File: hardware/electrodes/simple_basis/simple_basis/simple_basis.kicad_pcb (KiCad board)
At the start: 2 copper layers, 58.4 x 69.7 mm, 0 parts

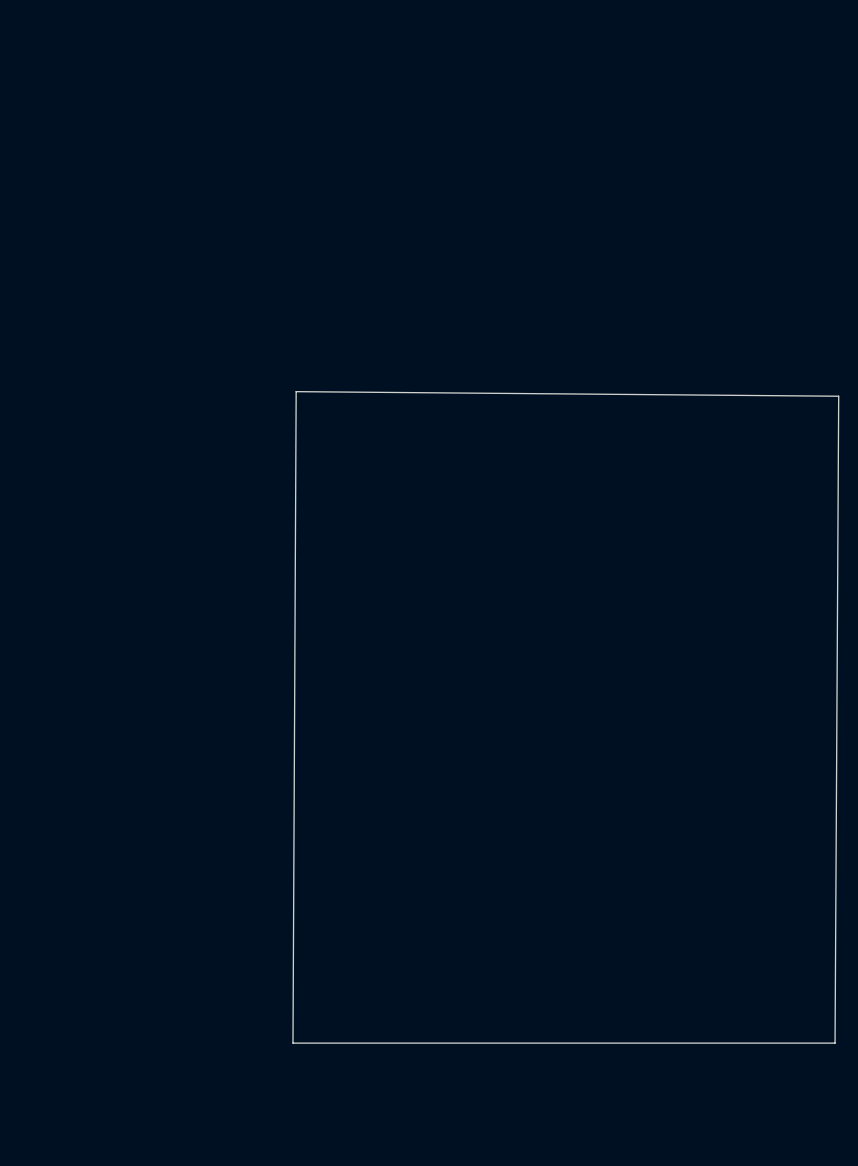
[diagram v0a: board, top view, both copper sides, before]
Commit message: Generating simple electrodes
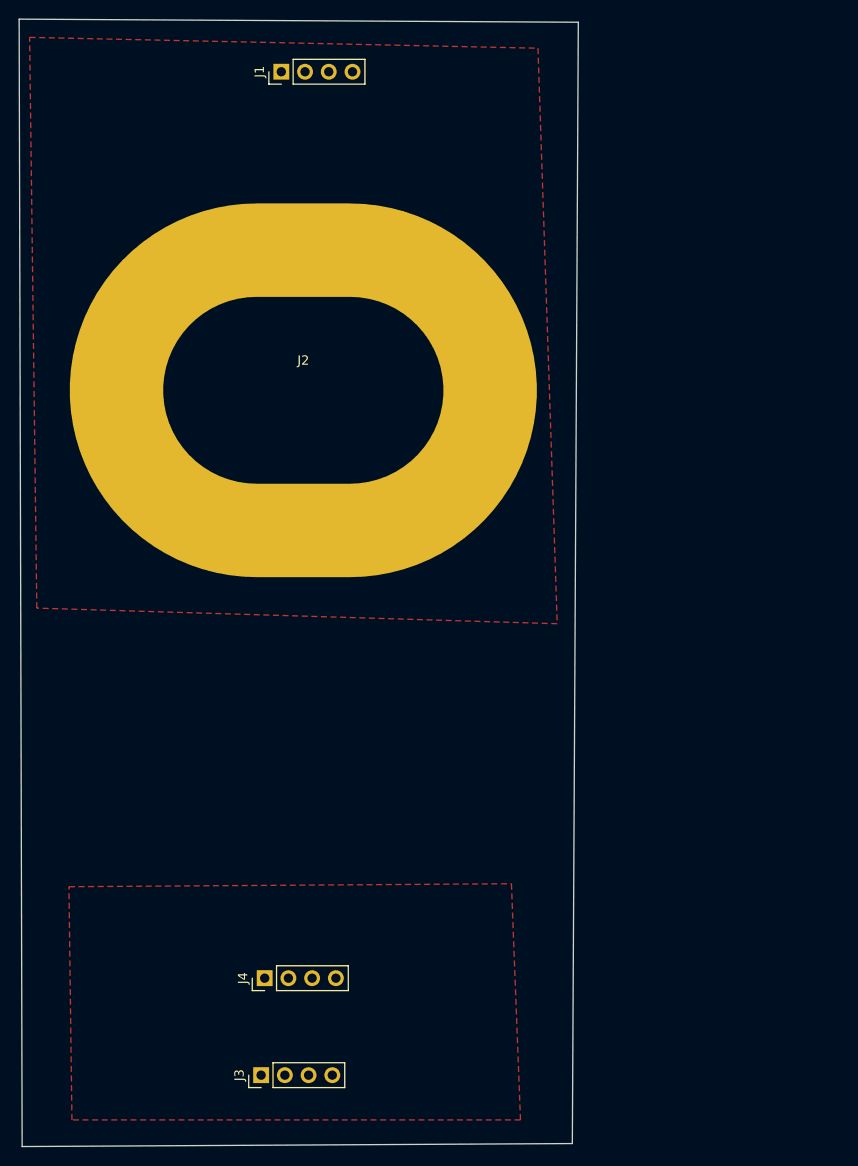
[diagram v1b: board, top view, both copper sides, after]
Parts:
- added J1: Conn_01x04_Male, Connector_PinHeader_2.54mm:PinHeader_1x04_P2.54mm_Vertical, F.Cu at (128.1, 45.5)
- added J2: Metallic_Electrode, electrodes:Electrode_ThroughHole_V0.1, F.Cu at (130.4, 75.9)
- added J3: Conn_01x04_Male, Connector_PinHeader_2.54mm:PinHeader_1x04_P2.54mm_Vertical, F.Cu at (125.9, 152.9)
- added J4: Conn_01x04_Male, Connector_PinHeader_2.54mm:PinHeader_1x04_P2.54mm_Vertical, F.Cu at (126.3, 142.6)
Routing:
- added copper zone on F.Cu, net Net-(J1-Pad1)
- added copper zone on F.Cu, net Net-(J3-Pad1)
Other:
- board size 58.4 x 69.7 mm -> 59.8 x 120.7 mm
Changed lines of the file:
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@@
     (tracks 0)
     (zones 0)
-    (modules 0)
-    (nets 1)
+    (modules 4)
+    (nets 3)
   )
   (page A4)
@@
     (visible_elements FFFFFF7F)
     (pcbplotparams
-      (layerselection 0x010fc_ffffffff)
+      (layerselection 0x010f0_ffffffff)
       (usegerberextensions false)
       (usegerberattributes true)
@@
       (outputformat 1)
       (mirror false)
-      (drillshape 1)
+      (drillshape 0)
       (scaleselection 1)
-      (outputdirectory ""))
+      (outputdirectory "../gerber/"))
   )
   (net 0 "")
+  (net 1 "Net-(J1-Pad1)")
+  (net 2 "Net-(J3-Pad1)")
   (net_class Default "This is the default net class."
     (clearance 0.2)
@@
     (uvia_dia 0.3)
     (uvia_drill 0.1)
-  )
-  (gr_line (start 129.65 79.79) (end 187.72 80.28) (layer Edge.Cuts) (width 0.1))
-  (gr_line (start 129.31 149.52) (end 129.65 79.79) (layer Edge.Cuts) (width 0.1))
-  (gr_line (start 187.33 149.52) (end 129.31 149.52) (layer Edge.Cuts) (width 0.1))
-  (gr_line (start 187.72 80.28) (end 187.33 149.52) (layer Edge.Cuts) (width 0.1))
+    (add_net "Net-(J1-Pad1)")
+    (add_net "Net-(J3-Pad1)")
+  )
+  (module Connector_PinHeader_2.54mm:PinHeader_1x04_P2.54mm_Vertical (layer F.Cu)
+    (at 126.28 142.57 90)
+    (descr "Through hole straight pin header, 1x04, 2.54mm pitch, single row")
+    (tags "Through hole pin header THT 1x04 2.54mm single row")
+    (fp_text reference J4 (at 0 -2.33 90) (layer F.SilkS)
+      (effects (font (size 1 1) (thickness 0.15)))
+    )
+    (fp_text value Conn_01x04_Male (at 0 9.95 90) (layer F.Fab)
+      (effects (font (size 1 1) (thickness 0.15)))
+    )
+    (fp_text user %R (at 0 3.81) (layer F.Fab)
+      (effects (font (size 1 1) (thickness 0.15)))
+    )
+    (fp_line (start -0.635 -1.27) (end 1.27 -1.27) (layer F.Fab) (width 0.1))
+    (fp_line (start 1.27 -1.27) (end 1.27 8.89) (layer F.Fab) (width 0.1))
+    (fp_line (start 1.27 8.89) (end -1.27 8.89) (layer F.Fab) (width 0.1))
+    (fp_line (start -1.27 8.89) (end -1.27 -0.635) (layer F.Fab) (width 0.1))
+    (fp_line (start -1.27 -0.635) (end -0.635 -1.27) (layer F.Fab) (width 0.1))
+    (fp_line (start -1.33 8.95) (end 1.33 8.95) (layer F.SilkS) (width 0.12))
+    (fp_line (start -1.33 1.27) (end -1.33 8.95) (layer F.SilkS) (width 0.12))
+    (fp_line (start 1.33 1.27) (end 1.33 8.95) (layer F.SilkS) (width 0.12))
+    (fp_line (start -1.33 1.27) (end 1.33 1.27) (layer F.SilkS) (width 0.12))
+    (fp_line (start -1.33 0) (end -1.33 -1.33) (layer F.SilkS) (width 0.12))
+    (fp_line (start -1.33 -1.33) (end 0 -1.33) (layer F.SilkS) (width 0.12))
+    (fp_line (start -1.8 -1.8) (end -1.8 9.4) (layer F.CrtYd) (width 0.05))
+    (fp_line (start -1.8 9.4) (end 1.8 9.4) (layer F.CrtYd) (width 0.05))
+    (fp_line (start 1.8 9.4) (end 1.8 -1.8) (layer F.CrtYd) (width 0.05))
+    (fp_line (start 1.8 -1.8) (end -1.8 -1.8) (layer F.CrtYd) (width 0.05))
+    (pad 4 thru_hole oval (at 0 7.62 90) (size 1.7 1.7) (drill 1) (layers *.Cu *.Mask)
+      (net 2 "Net-(J3-Pad1)"))
+    (pad 3 thru_hole oval (at 0 5.08 90) (size 1.7 1.7) (drill 1) (layers *.Cu *.Mask)
+      (net 2 "Net-(J3-Pad1)"))
+    (pad 2 thru_hole oval (at 0 2.54 90) (size 1.7 1.7) (drill 1) (layers *.Cu *.Mask)
+      (net 2 "Net-(J3-Pad1)"))
+    (pad 1 thru_hole rect (at 0 0 90) (size 1.7 1.7) (drill 1) (layers *.Cu *.Mask)
+      (net 2 "Net-(J3-Pad1)"))
+    (model ${KISYS3DMOD}/Connector_PinHeader_2.54mm.3dshapes/PinHeader_1x04_P2.54mm_Vertical.wrl
+      (at (xyz 0 0 0))
+      (scale (xyz 1 1 1))
+      (rotate (xyz 0 0 0))
+    )
+  )
+  (module Connector_PinHeader_2.54mm:PinHeader_1x04_P2.54mm_Vertical (layer F.Cu)
+    (at 125.9 152.95 90)
+    (descr "Through hole straight pin header, 1x04, 2.54mm pitch, single row")
+    (tags "Through hole pin header THT 1x04 2.54mm single row")
+    (fp_text reference J3 (at 0 -2.33 90) (layer F.SilkS)
+      (effects (font (size 1 1) (thickness 0.15)))
+    )
+    (fp_text value Conn_01x04_Male (at 0 9.95 90) (layer F.Fab)
+      (effects (font (size 1 1) (thickness 0.15)))
+    )
+    (fp_text user %R (at 0 3.81) (layer F.Fab)
+      (effects (font (size 1 1) (thickness 0.15)))
+    )
+    (fp_line (start -0.635 -1.27) (end 1.27 -1.27) (layer F.Fab) (width 0.1))
+    (fp_line (start 1.27 -1.27) (end 1.27 8.89) (layer F.Fab) (width 0.1))
+    (fp_line (start 1.27 8.89) (end -1.27 8.89) (layer F.Fab) (width 0.1))
+    (fp_line (start -1.27 8.89) (end -1.27 -0.635) (layer F.Fab) (width 0.1))
+    (fp_line (start -1.27 -0.635) (end -0.635 -1.27) (layer F.Fab) (width 0.1))
+    (fp_line (start -1.33 8.95) (end 1.33 8.95) (layer F.SilkS) (width 0.12))
+    (fp_line (start -1.33 1.27) (end -1.33 8.95) (layer F.SilkS) (width 0.12))
+    (fp_line (start 1.33 1.27) (end 1.33 8.95) (layer F.SilkS) (width 0.12))
+    (fp_line (start -1.33 1.27) (end 1.33 1.27) (layer F.SilkS) (width 0.12))
+    (fp_line (start -1.33 0) (end -1.33 -1.33) (layer F.SilkS) (width 0.12))
+    (fp_line (start -1.33 -1.33) (end 0 -1.33) (layer F.SilkS) (width 0.12))
+    (fp_line (start -1.8 -1.8) (end -1.8 9.4) (layer F.CrtYd) (width 0.05))
+    (fp_line (start -1.8 9.4) (end 1.8 9.4) (layer F.CrtYd) (width 0.05))
+    (fp_line (start 1.8 9.4) (end 1.8 -1.8) (layer F.CrtYd) (width 0.05))
+    (fp_line (start 1.8 -1.8) (end -1.8 -1.8) (layer F.CrtYd) (width 0.05))
+    (pad 4 thru_hole oval (at 0 7.62 90) (size 1.7 1.7) (drill 1) (layers *.Cu *.Mask)
+      (net 2 "Net-(J3-Pad1)"))
+    (pad 3 thru_hole oval (at 0 5.08 90) (size 1.7 1.7) (drill 1) (layers *.Cu *.Mask)
+      (net 2 "Net-(J3-Pad1)"))
+    (pad 2 thru_hole oval (at 0 2.54 90) (size 1.7 1.7) (drill 1) (layers *.Cu *.Mask)
+      (net 2 "Net-(J3-Pad1)"))
+    (pad 1 thru_hole rect (at 0 0 90) (size 1.7 1.7) (drill 1) (layers *.Cu *.Mask)
+      (net 2 "Net-(J3-Pad1)"))
+    (model ${KISYS3DMOD}/Connector_PinHeader_2.54mm.3dshapes/PinHeader_1x04_P2.54mm_Vertical.wrl
+      (at (xyz 0 0 0))
+      (scale (xyz 1 1 1))
+      (rotate (xyz 0 0 0))
+    )
+  )
+  (module electrodes:Electrode_ThroughHole_V0.1 (layer F.Cu)
+    (at 130.414999 75.944999)
+    (fp_text reference J2 (at 0 0.5) (layer F.SilkS)
+      (effects (font (size 1 1) (thickness 0.15)))
+    )
+    (fp_text value Metallic_Electrode (at 0 -0.5) (layer F.Fab)
+      (effects (font (size 1 1) (thickness 0.15)))
+    )
+    (pad 1 thru_hole oval (at 0 3.7) (size 50 40) (drill oval 30 20) (layers *.Cu *.Mask)
+      (net 1 "Net-(J1-Pad1)"))
+  )
+  (module Connector_PinHeader_2.54mm:PinHeader_1x04_P2.54mm_Vertical (layer F.Cu)
+    (at 128.06 45.55 90)
+    (descr "Through hole straight pin header, 1x04, 2.54mm pitch, single row")
+    (tags "Through hole pin header THT 1x04 2.54mm single row")
+    (fp_text reference J1 (at 0 -2.33 90) (layer F.SilkS)
+      (effects (font (size 1 1) (thickness 0.15)))
+    )
+    (fp_text value Conn_01x04_Male (at 0 9.95 90) (layer F.Fab)
+      (effects (font (size 1 1) (thickness 0.15)))
+    )
+    (fp_text user %R (at 0 3.81) (layer F.Fab)
+      (effects (font (size 1 1) (thickness 0.15)))
+    )
+    (fp_line (start -0.635 -1.27) (end 1.27 -1.27) (layer F.Fab) (width 0.1))
+    (fp_line (start 1.27 -1.27) (end 1.27 8.89) (layer F.Fab) (width 0.1))
+    (fp_line (start 1.27 8.89) (end -1.27 8.89) (layer F.Fab) (width 0.1))
+    (fp_line (start -1.27 8.89) (end -1.27 -0.635) (layer F.Fab) (width 0.1))
+    (fp_line (start -1.27 -0.635) (end -0.635 -1.27) (layer F.Fab) (width 0.1))
+    (fp_line (start -1.33 8.95) (end 1.33 8.95) (layer F.SilkS) (width 0.12))
+    (fp_line (start -1.33 1.27) (end -1.33 8.95) (layer F.SilkS) (width 0.12))
+    (fp_line (start 1.33 1.27) (end 1.33 8.95) (layer F.SilkS) (width 0.12))
+    (fp_line (start -1.33 1.27) (end 1.33 1.27) (layer F.SilkS) (width 0.12))
+    (fp_line (start -1.33 0) (end -1.33 -1.33) (layer F.SilkS) (width 0.12))
+    (fp_line (start -1.33 -1.33) (end 0 -1.33) (layer F.SilkS) (width 0.12))
+    (fp_line (start -1.8 -1.8) (end -1.8 9.4) (layer F.CrtYd) (width 0.05))
+    (fp_line (start -1.8 9.4) (end 1.8 9.4) (layer F.CrtYd) (width 0.05))
+    (fp_line (start 1.8 9.4) (end 1.8 -1.8) (layer F.CrtYd) (width 0.05))
+    (fp_line (start 1.8 -1.8) (end -1.8 -1.8) (layer F.CrtYd) (width 0.05))
+    (pad 4 thru_hole oval (at 0 7.62 90) (size 1.7 1.7) (drill 1) (layers *.Cu *.Mask)
+      (net 1 "Net-(J1-Pad1)"))
+    (pad 3 thru_hole oval (at 0 5.08 90) (size 1.7 1.7) (drill 1) (layers *.Cu *.Mask)
+      (net 1 "Net-(J1-Pad1)"))
+    (pad 2 thru_hole oval (at 0 2.54 90) (size 1.7 1.7) (drill 1) (layers *.Cu *.Mask)
+      (net 1 "Net-(J1-Pad1)"))
+    (pad 1 thru_hole rect (at 0 0 90) (size 1.7 1.7) (drill 1) (layers *.Cu *.Mask)
+      (net 1 "Net-(J1-Pad1)"))
+    (model ${KISYS3DMOD}/Connector_PinHeader_2.54mm.3dshapes/PinHeader_1x04_P2.54mm_Vertical.wrl
+      (at (xyz 0 0 0))
+      (scale (xyz 1 1 1))
+      (rotate (xyz 0 0 0))
+    )
+  )
+  (gr_line (start 100 39.92) (end 159.85 40.25) (layer Edge.Cuts) (width 0.1))
+  (gr_line (start 100.32 160.59) (end 100 39.92) (layer Edge.Cuts) (width 0.1))
+  (gr_line (start 159.21 160.27) (end 100.32 160.59) (layer Edge.Cuts) (width 0.1))
+  (gr_line (start 159.85 40.25) (end 159.21 160.27) (layer Edge.Cuts) (width 0.1))
+  (zone (net 1) (net_name "Net-(J1-Pad1)") (layer F.Cu) (hatch edge 0.508)
+    (connect_pads (clearance 0.4))
+    (min_thickness 0.2)
+    (fill yes (arc_segments 32) (thermal_gap 0.508) (thermal_bridge_width 0.508))
+    (polygon
+      (pts
+        (xy 155.53 43.03) (xy 157.59 104.63) (xy 101.89 102.96) (xy 101.12 41.87)
+      )
+    )
+  )
+  (zone (net 2) (net_name "Net-(J3-Pad1)") (layer F.Cu) (hatch edge 0.508)
+    (connect_pads (clearance 0.4))
+    (min_thickness 0.2)
+    (fill yes (arc_segments 32) (thermal_gap 0.508) (thermal_bridge_width 0.508))
+    (polygon
+      (pts
+        (xy 153.66 157.74) (xy 105.65 157.74) (xy 105.33 132.78) (xy 152.69 132.46)
+      )
+    )
+  )
 )
